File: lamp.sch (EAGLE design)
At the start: 63 parts, among them P1 10kΩ, P2 2MΩ

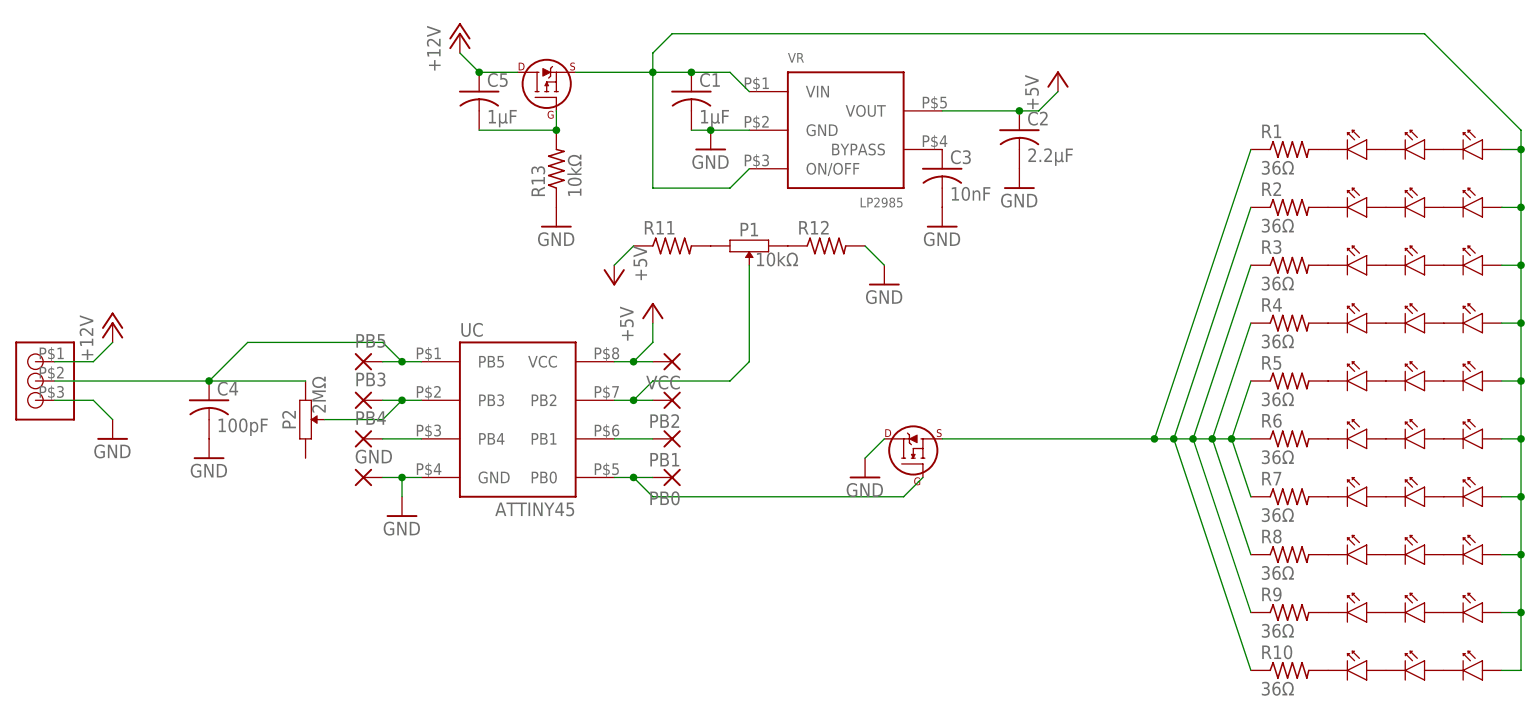
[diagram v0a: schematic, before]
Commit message: Fixed nfet that controls led channels. Added resistors to pwm control line. Adjusted nfet and pfet symbols.
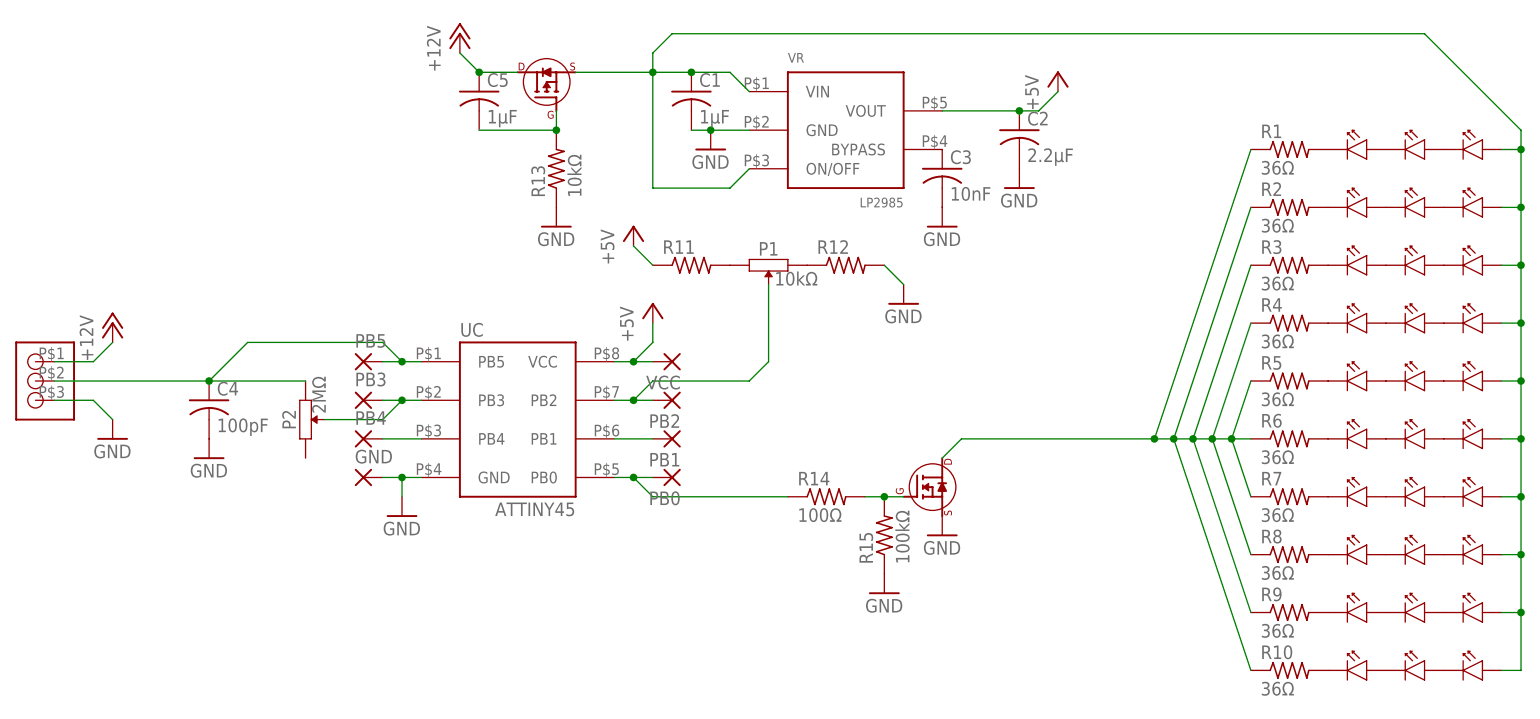
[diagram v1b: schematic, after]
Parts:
- added R14: 100Ω, Barebones-Arduino:RESISTOR-SMD
- added R15: 100kΩ, Barebones-Arduino:RESISTOR-SMD
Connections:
- new net N$15: F1.GATE, R14.2, R15.2
- net GND: now also F1.SOURCE, R15.1; no longer F1.DRAIN
- net N$33: now also F1.DRAIN; no longer F1.SOURCE
- net N$47: now also R14.1; no longer F1.GATE
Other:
- moved on the sheet: P1, R11, R12
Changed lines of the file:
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@@
 <part name="GND1" library=" Barebones-Arduino" deviceset="GND" device=""/>
 <part name="F1" library="lamp" deviceset="SI2318DS" device=""/>
+<part name="R14" library=" Barebones-Arduino" deviceset="RESISTOR" device="-SMD" value="100Ω"/>
+<part name="R15" library=" Barebones-Arduino" deviceset="RESISTOR" device="-SMD" value="100kΩ"/>
+<part name="GND10" library=" Barebones-Arduino" deviceset="GND" device=""/>
 </parts>
 <sheets>
@@
 <instance part="P+5" gate="1" x="-50.8" y="55.88"/>
 <instance part="GND7" gate="1" x="-50.8" y="40.64"/>
-<instance part="P1" gate="G$1" x="33.02" y="66.04" rot="R90"/>
-<instance part="R11" gate="G$1" x="22.86" y="66.04"/>
-<instance part="R12" gate="G$1" x="43.18" y="66.04"/>
-<instance part="P+1" gate="1" x="15.24" y="60.96" rot="R180"/>
-<instance part="GND8" gate="1" x="50.8" y="60.96"/>
+<instance part="P1" gate="G$1" x="35.56" y="63.5" rot="R90"/>
+<instance part="R11" gate="G$1" x="25.4" y="63.5"/>
+<instance part="R12" gate="G$1" x="45.72" y="63.5"/>
+<instance part="P+1" gate="1" x="17.78" y="68.58"/>
+<instance part="GND8" gate="1" x="53.34" y="58.42"/>
 <instance part="P2" gate="G$1" x="-25.4" y="43.18" rot="R180"/>
 <instance part="C4" gate="G$1" x="-38.1" y="45.72"/>
@@
 <instance part="R13" gate="G$1" x="7.62" y="76.2" rot="R90"/>
 <instance part="C5" gate="G$1" x="-2.54" y="86.36"/>
-<instance part="GND1" gate="1" x="48.26" y="35.56"/>
-<instance part="F1" gate="G$1" x="53.34" y="40.64"/>
+<instance part="GND1" gate="1" x="58.42" y="27.94"/>
+<instance part="F1" gate="G$1" x="58.42" y="35.56" rot="R270"/>
+<instance part="R14" gate="G$1" x="43.18" y="33.02"/>
+<instance part="R15" gate="G$1" x="50.8" y="27.94" rot="R90"/>
+<instance part="GND10" gate="1" x="50.8" y="20.32"/>
 </instances>
 <busses>
@@
 </segment>
 <segment>
-<pinref part="F1" gate="G$1" pin="DRAIN"/>
-<pinref part="GND1" gate="1" pin="GND"/>
-<wire x1="50.8" y1="40.64" x2="48.26" y2="38.1" width="0.1524" layer="91"/>
-</segment>
-<segment>
 <pinref part="R12" gate="G$1" pin="2"/>
 <pinref part="GND8" gate="1" pin="GND"/>
-<wire x1="48.26" y1="66.04" x2="50.8" y2="63.5" width="0.1524" layer="91"/>
+<wire x1="50.8" y1="63.5" x2="53.34" y2="60.96" width="0.1524" layer="91"/>
+</segment>
+<segment>
+<pinref part="F1" gate="G$1" pin="SOURCE"/>
+<pinref part="GND1" gate="1" pin="GND"/>
+</segment>
+<segment>
+<pinref part="R15" gate="G$1" pin="1"/>
+<pinref part="GND10" gate="1" pin="GND"/>
 </segment>
 </net>
@@
 <wire x1="17.78" y1="35.56" x2="20.32" y2="33.02" width="0.1524" layer="91"/>
 <junction x="17.78" y="35.56"/>
-<wire x1="20.32" y1="33.02" x2="53.34" y2="33.02" width="0.1524" layer="91"/>
-<pinref part="F1" gate="G$1" pin="GATE"/>
-<wire x1="53.34" y1="33.02" x2="55.88" y2="35.56" width="0.1524" layer="91"/>
+<pinref part="R14" gate="G$1" pin="1"/>
+<wire x1="20.32" y1="33.02" x2="38.1" y2="33.02" width="0.1524" layer="91"/>
 </segment>
 </net>
@@
 <pinref part="R11" gate="G$1" pin="1"/>
 <pinref part="P+1" gate="1" pin="+5V"/>
-<wire x1="17.78" y1="66.04" x2="15.24" y2="63.5" width="0.1524" layer="91"/>
+<wire x1="20.32" y1="63.5" x2="17.78" y2="66.04" width="0.1524" layer="91"/>
 </segment>
 </net>
@@
 <wire x1="17.78" y1="45.72" x2="20.32" y2="45.72" width="0.1524" layer="91"/>
 <wire x1="17.78" y1="45.72" x2="20.32" y2="48.26" width="0.1524" layer="91"/>
-<wire x1="20.32" y1="48.26" x2="30.48" y2="48.26" width="0.1524" layer="91"/>
+<wire x1="20.32" y1="48.26" x2="33.02" y2="48.26" width="0.1524" layer="91"/>
 <junction x="17.78" y="45.72"/>
-<wire x1="30.48" y1="48.26" x2="33.02" y2="50.8" width="0.1524" layer="91"/>
+<wire x1="33.02" y1="48.26" x2="35.56" y2="50.8" width="0.1524" layer="91"/>
 <pinref part="P1" gate="G$1" pin="P$2"/>
-<wire x1="33.02" y1="63.5" x2="33.02" y2="50.8" width="0.1524" layer="91"/>
+<wire x1="35.56" y1="60.96" x2="35.56" y2="50.8" width="0.1524" layer="91"/>
 </segment>
 </net>
@@
 <pinref part="R1" gate="G$1" pin="1"/>
 <wire x1="99.06" y1="78.74" x2="86.36" y2="40.64" width="0.1524" layer="91"/>
-<wire x1="86.36" y1="40.64" x2="58.42" y2="40.64" width="0.1524" layer="91"/>
+<pinref part="F1" gate="G$1" pin="DRAIN"/>
+<wire x1="86.36" y1="40.64" x2="60.96" y2="40.64" width="0.1524" layer="91"/>
+<wire x1="60.96" y1="40.64" x2="58.42" y2="38.1" width="0.1524" layer="91"/>
 <junction x="86.36" y="40.64"/>
-<pinref part="F1" gate="G$1" pin="SOURCE"/>
 </segment>
 </net>
@@
 </segment>
 </net>
+<net name="N$15" class="0">
+<segment>
+<pinref part="R14" gate="G$1" pin="2"/>
+<pinref part="R15" gate="G$1" pin="2"/>
+<pinref part="F1" gate="G$1" pin="GATE"/>
+<wire x1="50.8" y1="33.02" x2="53.34" y2="33.02" width="0.1524" layer="91"/>
+<junction x="50.8" y="33.02"/>
+<wire x1="50.8" y1="33.02" x2="48.26" y2="33.02" width="0.1524" layer="91"/>
+</segment>
+</net>

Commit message: Removed soft-start RC from reverse polarity protection fet F2. Removed solder mask holes from led vias so they will get tented instead.
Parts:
- removed C5: 1µF, Barebones-Arduino:CAPACITOR-SMD
- removed R15: 100kΩ, Barebones-Arduino:RESISTOR-SMD
- R13: value 10kΩ -> 100Ω
- R14: value 100Ω -> 100kΩ
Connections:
- removed net N$14: C5.2, F2.GATE, R13.2
- net +12V: no longer C5.1
- net GND: now also F2.GATE, R14.1; no longer R13.1, R15.1
- net N$15: now also R13.2; no longer R15.2
- net N$47: now also R13.1; no longer R14.1
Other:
- moved on the sheet: R13, R14
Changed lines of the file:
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@@
 <part name="C4" library=" Barebones-Arduino" deviceset="CAPACITOR" device="-SMD" value="100pF"/>
 <part name="GND9" library=" Barebones-Arduino" deviceset="GND" device=""/>
-<part name="R13" library=" Barebones-Arduino" deviceset="RESISTOR" device="-SMD" value="10kΩ"/>
-<part name="C5" library=" Barebones-Arduino" deviceset="CAPACITOR" device="-SMD" value="1µF"/>
 <part name="GND1" library=" Barebones-Arduino" deviceset="GND" device=""/>
 <part name="F1" library="lamp" deviceset="SI2318DS" device=""/>
-<part name="R14" library=" Barebones-Arduino" deviceset="RESISTOR" device="-SMD" value="100Ω"/>
-<part name="R15" library=" Barebones-Arduino" deviceset="RESISTOR" device="-SMD" value="100kΩ"/>
+<part name="R13" library=" Barebones-Arduino" deviceset="RESISTOR" device="-SMD" value="100Ω"/>
+<part name="R14" library=" Barebones-Arduino" deviceset="RESISTOR" device="-SMD" value="100kΩ"/>
 <part name="GND10" library=" Barebones-Arduino" deviceset="GND" device=""/>
 </parts>
@@
 <instance part="GND4" gate="1" x="58.42" y="68.58"/>
 <instance part="F2" gate="G$1" x="5.08" y="88.9"/>
-<instance part="GND6" gate="1" x="7.62" y="68.58"/>
+<instance part="GND6" gate="1" x="7.62" y="78.74"/>
 <instance part="U$32" gate="G$1" x="-58.42" y="50.8"/>
 <instance part="P+5" gate="1" x="-50.8" y="55.88"/>
@@
 <instance part="C4" gate="G$1" x="-38.1" y="45.72"/>
 <instance part="GND9" gate="1" x="-38.1" y="38.1"/>
-<instance part="R13" gate="G$1" x="7.62" y="76.2" rot="R90"/>
-<instance part="C5" gate="G$1" x="-2.54" y="86.36"/>
 <instance part="GND1" gate="1" x="58.42" y="27.94"/>
 <instance part="F1" gate="G$1" x="58.42" y="35.56" rot="R270"/>
-<instance part="R14" gate="G$1" x="43.18" y="33.02"/>
-<instance part="R15" gate="G$1" x="50.8" y="27.94" rot="R90"/>
+<instance part="R13" gate="G$1" x="43.18" y="33.02"/>
+<instance part="R14" gate="G$1" x="50.8" y="27.94" rot="R90"/>
 <instance part="GND10" gate="1" x="50.8" y="20.32"/>
 </instances>
@@
 </segment>
 <segment>
-<pinref part="GND6" gate="1" pin="GND"/>
-<pinref part="R13" gate="G$1" pin="1"/>
-</segment>
-<segment>
 <pinref part="R12" gate="G$1" pin="2"/>
 <pinref part="GND8" gate="1" pin="GND"/>
@@
 </segment>
 <segment>
-<pinref part="R15" gate="G$1" pin="1"/>
+<pinref part="R14" gate="G$1" pin="1"/>
 <pinref part="GND10" gate="1" pin="GND"/>
+</segment>
+<segment>
+<pinref part="F2" gate="G$1" pin="GATE"/>
+<wire x1="7.62" y1="81.28" x2="7.62" y2="83.82" width="0.1524" layer="91"/>
+<pinref part="GND6" gate="1" pin="GND"/>
 </segment>
 </net>
@@
 <wire x1="17.78" y1="35.56" x2="20.32" y2="33.02" width="0.1524" layer="91"/>
 <junction x="17.78" y="35.56"/>
-<pinref part="R14" gate="G$1" pin="1"/>
+<pinref part="R13" gate="G$1" pin="1"/>
 <wire x1="20.32" y1="33.02" x2="38.1" y2="33.02" width="0.1524" layer="91"/>
 </segment>
@@
 </segment>
 </net>
-<net name="N$14" class="0">
-<segment>
-<pinref part="F2" gate="G$1" pin="GATE"/>
-<pinref part="R13" gate="G$1" pin="2"/>
-<wire x1="7.62" y1="81.28" x2="7.62" y2="83.82" width="0.1524" layer="91"/>
-<pinref part="C5" gate="G$1" pin="2"/>
-<wire x1="-2.54" y1="81.28" x2="7.62" y2="81.28" width="0.1524" layer="91"/>
-<junction x="7.62" y="81.28"/>
-</segment>
-</net>
 <net name="N$33" class="0">
 <segment>
@@
 <segment>
 <pinref part="P+3" gate="1" pin="+12V"/>
-<pinref part="C5" gate="G$1" pin="1"/>
 <wire x1="-5.08" y1="91.44" x2="-2.54" y2="88.9" width="0.1524" layer="91"/>
 <pinref part="F2" gate="G$1" pin="DRAIN"/>
 <wire x1="-2.54" y1="88.9" x2="2.54" y2="88.9" width="0.1524" layer="91"/>
-<junction x="-2.54" y="88.9"/>
 </segment>
 <segment>
@@
 <net name="N$15" class="0">
 <segment>
+<pinref part="R13" gate="G$1" pin="2"/>
 <pinref part="R14" gate="G$1" pin="2"/>
-<pinref part="R15" gate="G$1" pin="2"/>
 <pinref part="F1" gate="G$1" pin="GATE"/>
 <wire x1="50.8" y1="33.02" x2="53.34" y2="33.02" width="0.1524" layer="91"/>
